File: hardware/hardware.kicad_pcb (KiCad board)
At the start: 2 copper layers, 81 x 60.5 mm, 213 parts, among them J1 USB_B_Micro, J2 RJ45_Hanrun_HR911105A_Horizon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, J3 Conn_02x05_Odd_Even, J4 Conn_02x03_Odd_Even, J5 Conn_01x02, U10 CH32V003F4P6, U11 CH32V003F4P6, U12 CH32V003F4P6, U13 CH32V003F4P6, U14 CH32V003F4P6, U15 CH32V003F4P6, U16 CH32V003F4P6, U17 CH32V003F4P6, U18 CH32V003F4P6, U19 CH32V003F4P6, U2 CH32V003F4P6, U20 CH32V003F4P6, U21 CH32V003F4P6, U22 CH32V003F4P6, U23 CH32V003F4P6, U24 CH32V003F4P6, U25 CH32V003F4P6, U26 CH32V003F4P6, U27 CH32V003F4P6, U28 CH32V307RCT6, U3 AMS1117-3.3, U4 CH340C, U5 CH32V003F4P6, U6 CH32V003F4P6, U7 CH32V003F4P6, U8 CH32V003F4P6, U9 CH32V003F4P6, Y1 Crystal_GND24

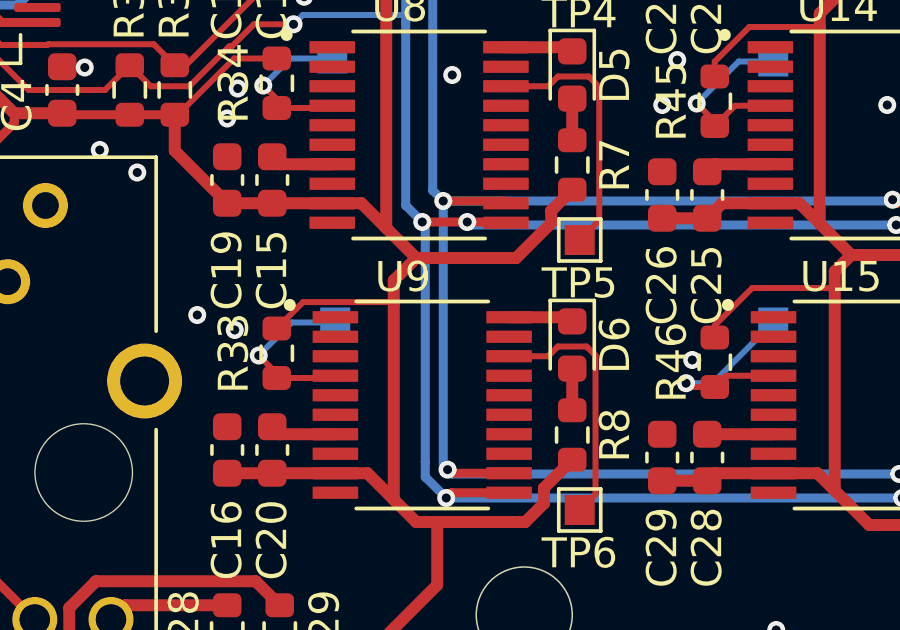
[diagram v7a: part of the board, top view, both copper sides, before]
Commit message: crystal to gnd
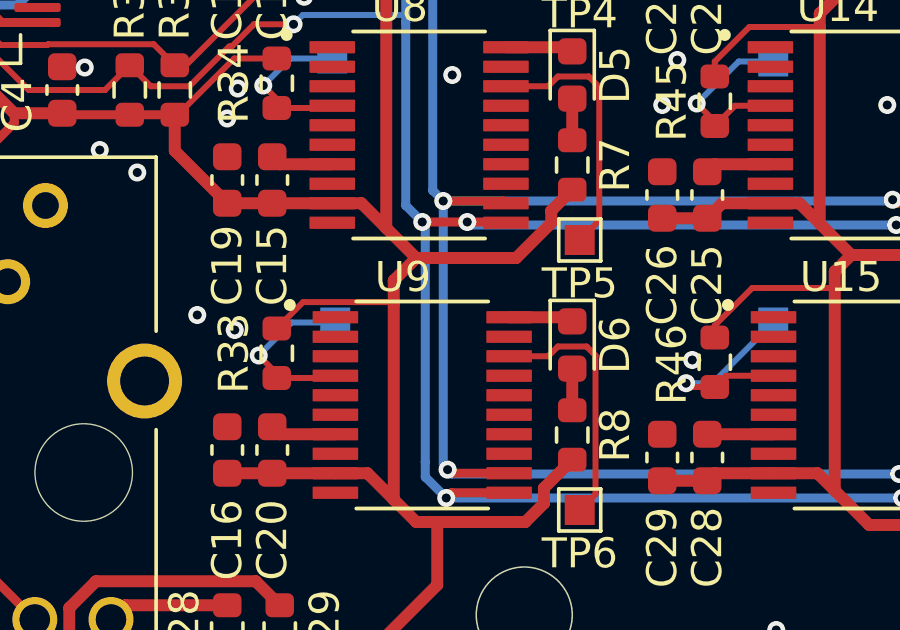
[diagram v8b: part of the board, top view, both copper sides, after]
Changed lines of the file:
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@@
 		(tags "capacitor")
 		(property "Reference" "C19"
-			(at -3 0 90)
+			(at -2.85 0 90)
 			(layer "F.SilkS")
 			(effects
@@
 		(tags "capacitor")
 		(property "Reference" "C15"
-			(at -3 0 90)
+			(at -2.85 0 90)
 			(layer "F.SilkS")
 			(effects
@@
 		(tags "resistor")
 		(property "Reference" "R46"
-			(at 0 -1.43 90)
+			(at -0.075 -1.43 90)
 			(layer "F.SilkS")
 			(effects
